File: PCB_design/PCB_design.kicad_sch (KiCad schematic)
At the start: 2 parts, among them U1 L298N

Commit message: Updated PCB Design
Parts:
- added C1, C2, C3: C, symbol Device:C
- added C4, C5, C6, C7: C_Polarized_US, symbol Device:C_Polarized_US
- added D1: LED, symbol Device:LED
- added D1, D2, D3, D4, D5, D6, D7, D8: 1N5400, Diode_THT:D_DO-201AD_P15.24mm_Horizontal, symbol Diode:1N5400
- added D9: D_Schottky, symbol Device:D_Schottky
- added L1: L, symbol Device:L
- added R1: R, symbol Device:R
- added R2, R3: R_US, symbol Device:R_US
- added U2: L7805, symbol Regulator_Linear:L7805
- added VR1: XL6009, XL6009:DPAK170P1435X465-6N, symbol XL6009:XL6009
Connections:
- net GND: now reaches U1.1 (SENSE_A)
- net GND: now also A1.29 (GND), A1.4 (GND), U1.11 (EnB), U1.15 (SENSE_B), U1.6 (EnA), U1.8 (GND), C2.2, C4.2, C5.2, C6.2, C7.2, D5.2 (A), D6.2 (A), D7.2 (A), D8.2 (A), R3.2, U2.2 (GND), VR1.1 (GND)
- net at U1.13 (OUT3): now also D2.2 (A), D7.1 (K)
- net at U1.14 (OUT4): now also D1.2 (A), D8.1 (K)
- net at U1.2 (OUT1): now also D4.2 (A), D5.1 (K)
- net at U1.3 (OUT2): now also D3.2 (A), D6.1 (K)
- net +5V: now reaches U1.4 (Vs)
- net +5V: now also C1.2, C2.1, C3.1, D1.1 (K), D1.1 (K), D2.1 (K), D3.1 (K), D4.1 (K)
- net at U1.5 (IN1): now also A1.19 (A0)
- net at U1.7 (IN2): now also A1.20 (A1)
- net +12V: now reaches U1.9 (Vss)
- net +12V: now also C6.1, C7.1, D9.1 (K), R2.1, U2.1 (IN)
- net at A1.30 (VIN): now also C3.2
- new net: C4.1, C5.1, L1.1, VR1.4 (VIN)
- new net: C1.1, R1.1, U2.3 (OUT)
- new net: D1.2 (A), R1.2
- new net: D9.2 (A), L1.2, VR1.3 (SW), VR1.6 (SW)
- new net: R2.2, R3.1, VR1.5 (FB)
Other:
- note added: "Arduino Nano"
- note added: "Boost Converter"
- note added: "L298N"
- note added: "V_out"
- moved on the sheet: A1, U1

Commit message: Added ICs for battery charging and battery charging protection to implement with Boost Converter on PCB.
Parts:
- added J1: USB_B, symbol Connector:USB_B
- added U3: TP4056, TP4056:SOP127P600X175-9N, symbol TP4056:TP4056
- added U4: DW01A, DW01A:SOT95P280X145-6N, symbol DW01A:DW01A
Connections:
- net +12V: no longer C6.1, C7.1, D9.1 (K), R2.1
- new net: C6.1, C7.1, D9.1 (K), R2.1
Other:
- note added: "Battery Charging Protection"
- note added: "Battery Port Charger w. Protection & Boost Converter"
- note added: "Linear Li-Po Charging IC"
- moved on the sheet: C4, C5, C6, C7, D9, L1, R2, R3, VR1

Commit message: Finished v0 of schematic
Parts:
- removed J1: USB_B, symbol Connector:USB_B
- added C10: 100nF, symbol Device:C
- added C8, C9: 10uF, symbol Device:C
- added GreenLED, RedLED: LED, symbol Device:LED
- added J1: USB_B_Micro, Connector_USB:USB_Mini-B_AdamTech_MUSB-B5-S-VT-TSMT-1_SMD_Vertical, symbol Connector:USB_B_Micro
- added Q1: FS8205A, FS8205A:SOP65P640X120-8N, symbol FS8205A:FS8205A
- added R4: R_Variable_US, symbol Device:R_Variable_US
- added R5, R6, R7: 1k, symbol Device:R_US
- added R8: 100, symbol Device:R_US
- added R_PROG: 1.2k, symbol Device:R_US
- D9: value D_Schottky -> 1N5824
- L1: value L -> 33uh/4A
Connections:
- net GND: now also U3.1 (TEMP), U3.3 (GND), C8.2, C9.2, J1.5 (GND), Q1.6, Q1.7, R7.2, R_PROG.2
- net VCC: now reaches C4.1, C5.1, L1.1, VR1.4 (VIN)
- net VCC: now also U3.5 (BAT), C9.1, R8.2
- net at U3.2 (PROG): now also R_PROG.1
- net at U3.4 (VCC): now also C8.1, J1.1 (VBUS)
- net Hold: now reaches U3.6 (~{STDBY})
- net Hold: now also R5.2
- net Charge: now reaches U3.7 (~{CHRG})
- net Charge: now also R6.2
- net at U3.8 (CE): now also GreenLED.2 (A), RedLED.2 (A)
- net Boost_Out: now reaches C6.1, C7.1, D9.1 (K), R2.1
- net at U4.1 (OD): now also Q1.4
- net at U4.2 (CS): now also R7.1
- net at U4.3 (OC): now also Q1.5
- net at U4.5 (VCC): now also C10.1, R8.1
- net Batt-: now reaches U4.6 (GND)
- net Batt-: now also C10.2, Q1.2, Q1.3
- new net: GreenLED.1 (K), R6.1
- new net: Q1.1, Q1.8
- new net: R5.1, RedLED.1 (K)
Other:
- note added: "105"
- note added: "220uF/50V"
- note added: "47uF/50V"
- note added: "MOSFET"
- note added: "Signal Generator Circuit"
- note added: "Vout = 1.25 * (1 + R2/R1)"
- moved on the sheet: A1, C1, C2, C3, C4, C5, D1, D2, D3, D4, D5, D6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

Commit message: Added most of the footprints and imported into PCB designer
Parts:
- removed C3: C, symbol Device:C
- removed GreenLED, RedLED: LED, symbol Device:LED
- removed R1: R, symbol Device:R
- removed R2: R_US, symbol Device:R_US
- added D10: RED_LED, LED_SMD:LED_0201_0603Metric_Pad0.64x0.40mm_HandSolder, symbol Device:LED
- added D11: GREEN_LED, LED_SMD:LED_0201_0603Metric_Pad0.64x0.40mm_HandSolder, symbol Device:LED
- added R9: 1k, Resistor_SMD:R_0603_1608Metric_Pad0.98x0.95mm_HandSolder, symbol Device:R_US
- C1: value C -> 220uF; footprint (none) -> Capacitor_SMD:C_0201_0603Metric_Pad0.64x0.40mm_HandSolder
- C10: footprint (none) -> Capacitor_SMD:C_0603_1608Metric_Pad1.08x0.95mm_HandSolder
- C2: value C -> 220uF; footprint (none) -> Capacitor_SMD:C_0603_1608Metric_Pad1.08x0.95mm_HandSolder
- C4, C5, C6, C7: footprint (none) -> Capacitor_SMD:CP_Elec_3x5.3
- C8, C9: footprint (none) -> Capacitor_SMD:C_0201_0603Metric_Pad0.64x0.40mm_HandSolder
- D1, D2, D3, D4, D5, D6, D7, D8: footprint Diode_THT:D_DO-201AD_P15.24mm_Horizontal -> Diode_SMD:D_0603_1608Metric_Pad1.05x0.95mm_HandSolder
- D17: renamed from D1; footprint (none) -> LED_SMD:LED_0201_0603Metric_Pad0.64x0.40mm_HandSolder
- D9: footprint (none) -> SS34:DIOM7959X265N
- L1: footprint (none) -> Inductor_SMD:L_7.3x7.3_H3.5
- R3: value R_US -> 1k; footprint (none) -> Resistor_SMD:R_0603_1608Metric_Pad0.98x0.95mm_HandSolder
- R4: footprint (none) -> Potentiometer_SMD:Potentiometer_Bourns_3269W_Vertical
- R5, R6, R7, R8: footprint (none) -> Resistor_SMD:R_0603_1608Metric_Pad0.98x0.95mm_HandSolder
- R_PROG1: renamed from R_PROG; footprint (none) -> Resistor_SMD:R_0603_1608Metric_Pad0.98x0.95mm_HandSolder
- U1: footprint Package_TO_SOT_THT:TO-220-15_P2.54x2.54mm_StaggerOdd_Lead4.58mm_Vertical -> L298N:TO127P2020X500X2100-15
- U2: footprint (none) -> L78M05CDT:VREG_L78M05CDT
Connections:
- net +12V is gone; now on net Boost_Out: U1.9 (Vss), U2.1 (IN)
- net +5V: now also A1.30 (VIN)
- net Boost_Out: now also R4.1
- net at R6.1: now also D11.1 (K)
- net at U3.8 (CE): now also D10.2 (A), D11.2 (A)
- net OUT2: now reaches D3.2 (A), D6.1 (K), U1.3 (OUT2)
- net at C1.1, U2.3 (OUT): now also R9.1
- net OUT3: now reaches D2.2 (A), D7.1 (K), U1.13 (OUT3)
- net OUT4: now reaches D1.2 (A), D8.1 (K), U1.14 (OUT4)
- net OUT1: now reaches D4.2 (A), D5.1 (K), U1.2 (OUT1)
- net at R5.1: now also D10.1 (K)
- net at D17.2 (A): now also R9.2
- net at R3.1, VR1.5 (FB): now also R4.2
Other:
- moved on the sheet: R4

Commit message: Progress on PCB, added different capacitors, continued routing
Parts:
- added J4: Conn_01x02_Pin, Connector_Hirose:Hirose_DF13-02P-1.25DS_1x02_P1.25mm_Horizontal, symbol Connector:Conn_01x02_Pin
- C1: footprint Capacitor_SMD:C_0201_0603Metric_Pad0.64x0.40mm_HandSolder -> MAL215097001E3-KiCad:CAPAE1050X1050N
- C2: footprint Capacitor_SMD:C_0603_1608Metric_Pad1.08x0.95mm_HandSolder -> MAL215097001E3-KiCad:CAPAE1050X1050N
- C4: footprint Capacitor_SMD:CP_Elec_3x5.3 -> UUD1H221MNL1GS:CAPAE1030X1080N
- C5, C6, C7: footprint Capacitor_SMD:CP_Elec_3x5.3 -> MAL215097001E3-KiCad:CAPAE1050X1050N
- R4: value R_Variable_US -> 10-25k; footprint Potentiometer_SMD:Potentiometer_Bourns_3269W_Vertical -> Potentiometer_SMD:Potentiometer_Bourns_3224X_Vertical
- renumbered D8 to D2, D2 to D3, D7 to D4, D3 to D5, D4 to D7, D5 to D8
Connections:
- net Batt-: now also J4.1 (Pin_1)
- net VCC: now also J4.2 (Pin_2)
- net at U1.5 (IN1): now also A1.20 (A1); no longer A1.19 (A0)
- net at U1.7 (IN2): now also A1.19 (A0); no longer A1.20 (A1)
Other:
- moved on the sheet: D9

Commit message: Finished routing of PCB, v0
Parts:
- C1, C2, C7: footprint MAL215097001E3-KiCad:CAPAE1050X1050N -> Capacitor_220uF35V_smaller:CAPAE1050X1050N
- C4: footprint UUD1H221MNL1GS:CAPAE1030X1080N -> Capacitor_220uF35V_smaller:CAPAE1050X1050N
- C5: footprint MAL215097001E3-KiCad:CAPAE1050X1050N -> Capacitor_SMD:C_0201_0603Metric_Pad0.64x0.40mm_HandSolder
- C6: footprint MAL215097001E3-KiCad:CAPAE1050X1050N -> Capacitor_SMD:C_0603_1608Metric_Pad1.08x0.95mm_HandSolder
- D9: value 1N5824 -> SS34; footprint SS34:DIOM7959X265N -> KiCad:DIOM8059X256N
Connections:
- net Batt- is gone; now on net GND: C10.2, J4.1 (Pin_1), Q1.2, Q1.3, U4.6 (GND)
- net at U1.5 (IN1): now also A1.19 (A0); no longer A1.20 (A1)
- net at U1.7 (IN2): now also A1.20 (A1); no longer A1.19 (A0)
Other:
- moved on the sheet: A1, C1, C10, C2, C4, C5, C6, C7, C8, C9, D1, D10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

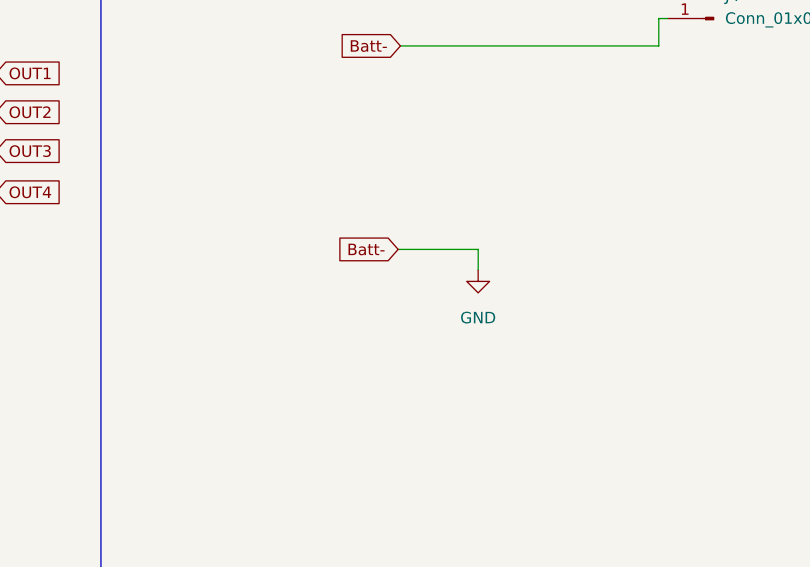
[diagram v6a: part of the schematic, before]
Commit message: Removed GND to Bat- connection and rereouted
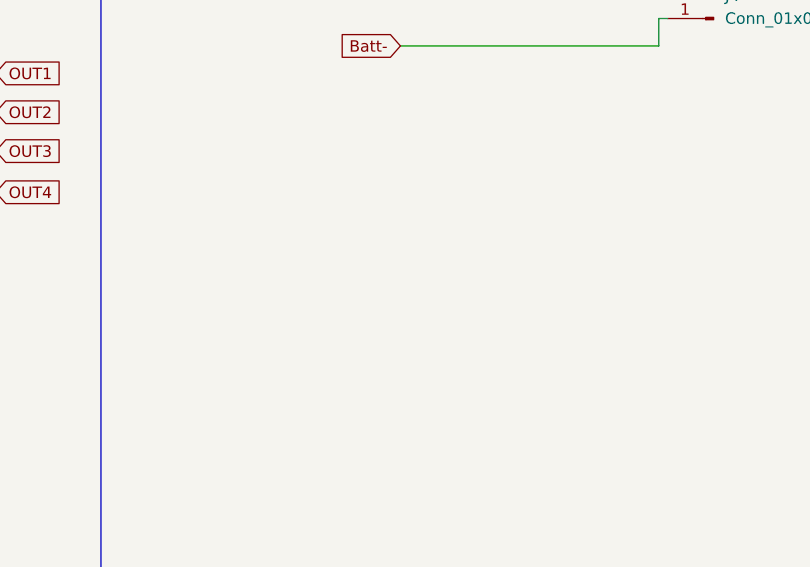
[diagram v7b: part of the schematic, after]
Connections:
- net GND: no longer C10.2, J4.1 (Pin_1), Q1.2, Q1.3, U4.6 (GND)
- new net Batt-: C10.2, J4.1 (Pin_1), Q1.2, Q1.3, U4.6 (GND)
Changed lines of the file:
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@@
-    (stroke (width 0) (type default))
-  )
-  (wire (pts (xy 246.126 104.14) (xy 255.016 104.14))
     (stroke (width 0) (type default))
   )
@@
   )
   (wire (pts (xy 164.592 86.106) (xy 164.592 88.392))
-    (stroke (width 0) (type default))
-  )
-  (wire (pts (xy 255.016 104.14) (xy 255.016 106.426))
     (stroke (width 0) (type default))
   )
@@
     (property "Intersheetrefs" "${INTERSHEET_REFS}" (at 209.1659 97.79 0)
       (effects (font (size 1.27 1.27)) (justify left) hide)
-    )
-  )
-  (global_label "Batt-" (shape input) (at 246.126 104.14 180) (fields_autoplaced)
-    (effects (font (size 1.27 1.27)) (justify right))
-    (property "Intersheetrefs" "${INTERSHEET_REFS}" (at 237.7774 104.14 0)
-      (effects (font (size 1.27 1.27)) (justify right) hide)
     )
   )
@@
         )
       )
-    )
-  )
-  (symbol (lib_id "power:GND") (at 255.016 106.426 0) (unit 1)
-    (in_bom yes) (on_board yes) (dnp no) (fields_autoplaced)
-    (property "Reference" "#PWR03" (at 255.016 112.776 0)
-      (effects (font (size 1.27 1.27)) hide)
-    )
-    (property "Value" "GND" (at 255.016 111.76 0)
-      (effects (font (size 1.27 1.27)))
-    )
-    (property "Footprint" "" (at 255.016 106.426 0)
-      (effects (font (size 1.27 1.27)) hide)
-    )
-    (property "Datasheet" "" (at 255.016 106.426 0)
-      (effects (font (size 1.27 1.27)) hide)
-    )
-    (pin "1")
-    (instances
-      (project "PCB_design"
-        (path "/e20d998c-6b71-47bf-8925-8b75746bc902"
-          (reference "#PWR03") (unit 1)
-        )
-      )

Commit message: Fixed issues surrounding wiring, Vss to Vs for 12V, CE actually enabled
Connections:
- net +5V: now also A1.27 (+5V), U1.11 (EnB), U1.6 (EnA); no longer A1.30 (VIN), C1.2, C2.1, D1.1 (K), D17.1 (K), D3.1 (K), D5.1 (K), D7.1 (K), U1.4 (Vs)
- net Boost_Out: now also U1.4 (Vs); no longer U1.9 (Vss)
- net GND: now also D17.1 (K), U3.9 (EP); no longer U1.11 (EnB), U1.6 (EnA)
- net at D10.2 (A), D11.2 (A), U3.8 (CE): now also C8.1, J1.1 (VBUS), U3.4 (VCC)
- net at U1.10 (IN3): now also A1.21 (A2)
- net at U1.12 (IN4): now also A1.22 (A3)
- new net: C1.2, C2.1, D1.1 (K), D3.1 (K), D5.1 (K), D7.1 (K), U1.9 (Vss)
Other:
- moved on the sheet: C10, D17, Q1, R7, R8, U4
